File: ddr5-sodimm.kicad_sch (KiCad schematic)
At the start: 31 parts, among them J2 Bus_DDR5_SODIMM_Amphenol_1016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, Q10 BSS138PW, Q11 BSS138PW, Q9 BSS138PW, SW3 SW_KMR211NGLFS_SMD

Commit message: Changing SO-DIMM sch to UDIMM
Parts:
- removed R23, R25: R_47k_0402, antmicro-footprints:R_0402_1005Metric, symbol antmicroResistors0402:R_47k_0402
- removed R24, R26, R27, R28, R29, R30, R32, R33, R34, R35: R_0R_0402, antmicro-footprints:R_0402_1005Metric, symbol antmicroResistors0402:R_0R_0402
- added unit 4 of J2
- J2: footprint antmicro-footprints:Bus_DDR5_SODIMM_Amphenol_10161033-002RHLF -> sodimm-ddr5-tester-footprints:Bus_DDR5_SODIMM_Amphenol_10161033-002RHLF; symbol antmicroMemoryConnectorsPCCardSockets:Bus_DDR5_SODIMM_Amphenol_10161033-002RHLF_CUSTOM_2xDetectPin -> sodimm-ddr5-tester-lib:Bus_DDR5_UDIMM_Amphenol; Author Antmicro -> HimaSava; MPN 10161033-002RHLF -> DDR503112007K
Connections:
- net RFU1 is gone; now on net DDR.SDA: J2.5 (HSDA)
- net +5V: now also J2.145 (VIN_BULK), J2.146 (VIN_BULK), J2.2 (VIN_BULK); no longer J2.3 (VIN_BULK)
- net A.CA0: now also J2.60 (CA0_A); no longer J2.107 (CA0_A)
- net A.CA1: now also J2.204 (CA1_A); no longer J2.109 (CA1_A)
- net A.CA10: now also J2.67 (CA10_A); no longer J2.125 (CA10_A)
- net A.CA11: now also J2.211 (CA11_A); no longer J2.126 (CA11_A)
- net A.CA12: now also J2.69 (CA12_A); no longer J2.127 (CA12_A)
- net A.CA2: now also J2.61 (CA2_A); no longer J2.113 (CA2_A)
- net A.CA3: now also J2.205 (CA3_A); no longer J2.114 (CA3_A)
- net A.CA4: now also J2.63 (CA4_A); no longer J2.115 (CA4_A)
- net A.CA5: now also J2.207 (CA5_A); no longer J2.116 (CA5_A)
- net A.CA6: now also J2.64 (CA6_A); no longer J2.119 (CA6_A)
- net A.CA7: now also J2.208 (CA7_A); no longer J2.120 (CA7_A)
- net A.CA8: now also J2.66 (CA8_A); no longer J2.121 (CA8_A)
- net A.CA9: now also J2.210 (CA9_A); no longer J2.122 (CA9_A)
- net A.CB0: now also J2.51 (CB0_A); no longer J2.95 (CB0_A)
- net A.CB1: now also J2.53 (CB1_A); no longer J2.96 (CB1_A)
- net A.CB2: now also J2.196 (CB2_A); no longer J2.99 (CB2_A)
- net A.CB3: now also J2.198 (CB3_A); no longer J2.103 (CB3_A)
- net A.CK0_N: now also J2.73 (CK0_A_c); no longer J2.133 (CK0_A_c)
- net A.CK0_P: now also J2.72 (CK0_A_t); no longer J2.131 (CK0_A_t)
- net A.CK1_N: now also J2.217 (CK1_A_c); no longer J2.134 (CK1_A_c)
- net A.CK1_P: now also J2.216 (CK1_A_t); no longer J2.132 (CK1_A_t)
- net A.DQ0: now also J2.9 (DQ0_A); no longer J2.11 (DQ0_A)
- net A.DQ1: now also J2.11 (DQ1_A); no longer J2.12 (DQ1_A)
- net A.DQ10: now also J2.164 (DQ10_A); no longer J2.35 (DQ10_A)
- net A.DQ11: now also J2.166 (DQ11_A); no longer J2.38 (DQ11_A)
- net A.DQ12: now also J2.26 (DQ12_A); no longer J2.45 (DQ12_A)
- net A.DQ13: now also J2.28 (DQ13_A); no longer J2.46 (DQ13_A)
- net A.DQ14: now also J2.171 (DQ14_A); no longer J2.49 (DQ14_A)
- net A.DQ15: now also J2.173 (DQ15_A); no longer J2.50 (DQ15_A)
- net A.DQ16: now also J2.30 (DQ16_A); no longer J2.53 (DQ16_A)
- net A.DQ17: now also J2.32 (DQ17_A); no longer J2.54 (DQ17_A)
- net A.DQ18: now also J2.175 (DQ18_A); no longer J2.57 (DQ18_A)
- net A.DQ19: now also J2.177 (DQ19_A); no longer J2.58 (DQ19_A)
- net A.DQ2: now also J2.154 (DQ2_A); no longer J2.15 (DQ2_A)
- net A.DQ20: now also J2.37 (DQ20_A); no longer J2.65 (DQ20_A)
- net A.DQ21: now also J2.39 (DQ21_A); no longer J2.68 (DQ21_A)
- net A.DQ22: now also J2.181 (DQ22_A); no longer J2.69 (DQ22_A)
- net A.DQ23: now also J2.183 (DQ23_A); no longer J2.72 (DQ23_A)
- net A.DQ24: now also J2.41 (DQ24_A); no longer J2.73 (DQ24_A)
- net A.DQ25: now also J2.43 (DQ25_A); no longer J2.76 (DQ25_A)
- net A.DQ26: now also J2.185 (DQ26_A); no longer J2.77 (DQ26_A)
- net A.DQ27: now also J2.187 (DQ27_A); no longer J2.80 (DQ27_A)
- net A.DQ28: now also J2.47 (DQ28_A); no longer J2.87 (DQ28_A)
- net A.DQ29: now also J2.49 (DQ29_A); no longer J2.88 (DQ29_A)
- net A.DQ3: now also J2.156 (DQ3_A); no longer J2.16 (DQ3_A)
- net A.DQ30: now also J2.192 (DQ30_A); no longer J2.91 (DQ30_A)
- net A.DQ31: now also J2.194 (DQ31_A); no longer J2.92 (DQ31_A)
- net A.DQ4: now also J2.16 (DQ4_A); no longer J2.23 (DQ4_A)
- net A.DQ5: now also J2.18 (DQ5_A); no longer J2.26 (DQ5_A)
- net A.DQ6: now also J2.160 (DQ6_A); no longer J2.27 (DQ6_A)
- net A.DQ7: now also J2.162 (DQ7_A); no longer J2.30 (DQ7_A)
- net A.DQ8: now also J2.20 (DQ8_A); no longer J2.31 (DQ8_A)
- net A.DQ9: now also J2.22 (DQ09_A); no longer J2.34 (DQ09_A)
- net A.DQS0_N: now also J2.13 (DQS0_A_C); no longer J2.20 (DQS0_A_C)
- net A.DQS0_P: now also J2.14 (DQS0_A_t); no longer J2.22 (DQS0_A_t)
- net A.DQS1_N: now also J2.168 (DQS1_A_C); no longer J2.39 (DQS1_A_C)
- net A.DQS1_P: now also J2.169 (DQS1_A_t); no longer J2.41 (DQS1_A_t)
- net A.DQS2_N: now also J2.34 (DQS2_A_C); no longer J2.62 (DQS2_A_C)
- net A.DQS2_P: now also J2.35 (DQS2_A_t); no longer J2.64 (DQS2_A_t)
- net A.DQS3_N: now also J2.189 (DQS3_A_C); no longer J2.81 (DQS3_A_C)
- net A.DQS3_P: now also J2.190 (DQS3_A_t); no longer J2.83 (DQS3_A_t)
- net A.DQS4_N: now also J2.55 (DQS4_A_c); no longer J2.100 (DQS4_A_c)
- net A.DQS4_P: now also J2.56 (DQS4_A_t); no longer J2.102 (DQS4_A_t)
- net A.~{CS0}: now also J2.58 (CS0_A_n); no longer J2.106 (CS0_A_n)
- net A.~{CS1}: now also J2.202 (CS1_A_n); no longer J2.110 (CS1_A_n)
- net A.~{DM0}: now also J2.158 (DM0_A_n); no longer J2.19 (DM0_A_n)
- net A.~{DM1}: now also J2.24 (DM1_A_n); no longer J2.42 (DM1_A_n)
- net A.~{DM2}: now also J2.179 (DM2_A_n); no longer J2.61 (DM2_A_n)
- net A.~{DM3}: now also J2.45 (DM3_A_n); no longer J2.84 (DM3_A_n)
- net B.CA0: now also J2.91 (CA0_B); no longer J2.164 (CA0_B)
- net B.CA1: now also J2.235 (CA1_B); no longer J2.162 (CA1_B)
- net B.CA10: now also J2.84 (CA10_B); no longer J2.146 (CA10_B)
- net B.CA11: now also J2.228 (CA11_B); no longer J2.145 (CA11_B)
- net B.CA12: now also J2.82 (CA12_B); no longer J2.144 (CA12_B)
- net B.CA2: now also J2.90 (CA2_B); no longer J2.158 (CA2_B)
- net B.CA3: now also J2.234 (CA3_B); no longer J2.157 (CA3_B)
- net B.CA4: now also J2.88 (CA4_B); no longer J2.156 (CA4_B)
- net B.CA5: now also J2.232 (CA5_B); no longer J2.155 (CA5_B)
- net B.CA6: now also J2.87 (CA6_B); no longer J2.152 (CA6_B)
- net B.CA7: now also J2.231 (CA7_B); no longer J2.151 (CA7_B)
- net B.CA8: now also J2.85 (CA8_B); no longer J2.150 (CA8_B)
- net B.CA9: now also J2.229 (CA9_B); no longer J2.149 (CA9_B)
- net B.CB0: now also J2.97 (CB0_B); no longer J2.168 (CB0_B)
- net B.CB1: now also J2.99 (CB1_B); no longer J2.172 (CB1_B)
- net B.CB2: now also J2.242 (CB2_B); no longer J2.176 (CB2_B)
- net B.CB3: now also J2.244 (CB3_B); no longer J2.175 (CB3_B)
- net B.CK0_N: now also J2.79 (CK0_B_c); no longer J2.139 (CK0_B_c)
- net B.CK0_P: now also J2.78 (CK0_B_t); no longer J2.137 (CK0_B_t)
- net B.CK1_N: now also J2.223 (CK1_B_C); no longer J2.140 (CK1_B_C)
- net B.CK1_P: now also J2.222 (CK1_B_t); no longer J2.138 (CK1_B_t)
- net B.DQ0: now also J2.101 (DQ0_B); no longer J2.179 (DQ0_B)
- net B.DQ1: now also J2.103 (DQ1_B); no longer J2.180 (DQ1_B)
- net B.DQ10: now also J2.256 (DQ10_B); no longer J2.203 (DQ10_B)
- net B.DQ11: now also J2.258 (DQ11_B); no longer J2.206 (DQ11_B)
- net B.DQ12: now also J2.118 (DQ12_B); no longer J2.213 (DQ12_B)
- net B.DQ13: now also J2.120 (DQ13_B); no longer J2.214 (DQ13_B)
- net B.DQ14: now also J2.263 (DQ14_B); no longer J2.217 (DQ14_B)
- net B.DQ15: now also J2.265 (DQ15_B); no longer J2.218 (DQ15_B)
- net B.DQ16: now also J2.122 (DQ16_B); no longer J2.221 (DQ16_B)
- net B.DQ17: now also J2.124 (DQ17_B); no longer J2.222 (DQ17_B)
- net B.DQ18: now also J2.267 (DQ18_B); no longer J2.225 (DQ18_B)
- net B.DQ19: now also J2.269 (DQ19_B); no longer J2.226 (DQ19_B)
- net B.DQ2: now also J2.246 (DQ2_B); no longer J2.183 (DQ2_B)
- net B.DQ20: now also J2.129 (DQ20_B); no longer J2.233 (DQ20_B)
- net B.DQ21: now also J2.131 (DQ21_B); no longer J2.236 (DQ21_B)
- net B.DQ22: now also J2.273 (DQ22_B); no longer J2.237 (DQ22_B)
- net B.DQ23: now also J2.275 (DQ23_B); no longer J2.240 (DQ23_B)
- net B.DQ24: now also J2.133 (DQ24_B); no longer J2.241 (DQ24_B)
- net B.DQ25: now also J2.135 (DQ25_B); no longer J2.244 (DQ25_B)
- net B.DQ26: now also J2.277 (DQ26_B); no longer J2.245 (DQ26_B)
- net B.DQ27: now also J2.279 (DQ27_B); no longer J2.248 (DQ27_B)
- net B.DQ28: now also J2.139 (DQ28_B); no longer J2.255 (DQ28_B)
- net B.DQ29: now also J2.141 (DQ29_B); no longer J2.256 (DQ29_B)
- net B.DQ3: now also J2.248 (DQ3_B); no longer J2.184 (DQ3_B)
- net B.DQ30: now also J2.284 (DQ30_B); no longer J2.259 (DQ30_B)
- net B.DQ31: now also J2.286 (DQ31_B); no longer J2.260 (DQ31_B)
- net B.DQ4: now also J2.108 (DQ4_B); no longer J2.191 (DQ4_B)
- net B.DQ5: now also J2.110 (DQ5_B); no longer J2.194 (DQ5_B)
- net B.DQ6: now also J2.252 (DQ6_B); no longer J2.195 (DQ6_B)
- net B.DQ7: now also J2.254 (DQ7_B); no longer J2.198 (DQ7_B)
- net B.DQ8: now also J2.112 (DQ8_B); no longer J2.199 (DQ8_B)
- net B.DQ9: now also J2.114 (DQ9_B); no longer J2.202 (DQ9_B)
- net B.DQS0_N: now also J2.105 (DQS0_B_C); no longer J2.188 (DQS0_B_C)
- net B.DQS0_P: now also J2.106 (DQS0_B_t); no longer J2.190 (DQS0_B_t)
- net B.DQS1_N: now also J2.260 (DQS1_B_C); no longer J2.207 (DQS1_B_C)
- net B.DQS1_P: now also J2.261 (DQS1_B_t); no longer J2.209 (DQS1_B_t)
- net B.DQS2_N: now also J2.126 (DQS2_B_C); no longer J2.230 (DQS2_B_C)
- net B.DQS2_P: now also J2.127 (DQS2_B_t); no longer J2.232 (DQS2_B_t)
- net B.DQS3_N: now also J2.281 (DQS3_B_c); no longer J2.249 (DQS3_B_c)
- net B.DQS3_P: now also J2.282 (DQS3_B_t); no longer J2.251 (DQS3_B_t)
- net B.DQS4_N: now also J2.239 (DQS4_B_c); no longer J2.169 (DQS4_B_c)
- net B.DQS4_P: now also J2.240 (DQS4_B_T); no longer J2.171 (DQS4_B_T)
- net B.~{CS0}: now also J2.93 (CS0_B_n); no longer J2.161 (CS0_B_n)
- net B.~{CS1}: now also J2.237 (CS1_B_N); no longer J2.165 (CS1_B_N)
- net B.~{DM0}: now also J2.250 (DM0_B_n); no longer J2.187 (DM0_B_n)
- net B.~{DM1}: now also J2.116 (DM1_B_n); no longer J2.210 (DM1_B_n)
- net B.~{DM2}: now also J2.271 (DM2_B_n); no longer J2.229 (DM2_B_n)
- net B.~{DM3}: now also J2.137 (DM3_B_n); no longer J2.252 (DM3_B_n)
- net Control.~{ALERT}: now also J2.200 (ALERT_n); no longer J2.108 (ALERT_n)
- net Control.~{RESET}: now also J2.95 (RESET_n); no longer J2.163 (RESET_n)
- net DDR.SDA: no longer J2.6 (HSDA)
- net GND: now also J2.10 (Vss), J2.100 (Vss), J2.102 (Vss), J2.104 (Vss), J2.107 (Vss), J2.109 (Vss), J2.111 (Vss), J2.113 (Vss), J2.115 (Vss), J2.117 (Vss), J2.119 (Vss), J2.12 (Vss), J2.121 (Vss), J2.123 (Vss), J2.125 (Vss), J2.128 (Vss), J2.130 (Vss), J2.132 (Vss), J2.134 (Vss), J2.136 (Vss), J2.138 (Vss), J2.140 (Vss), J2.142 (Vss), J2.15 (Vss), J2.150 (Vss), J2.153 (Vss), J2.155 (Vss), J2.157 (Vss), J2.159 (Vss), J2.161 (Vss), J2.163 (Vss), J2.165 (Vss), J2.167 (Vss), J2.17 (Vss), J2.170 (Vss), J2.172 (Vss), J2.174 (Vss), J2.176 (Vss), J2.178 (Vss), J2.180 (Vss), J2.182 (Vss), J2.184 (Vss), J2.186 (Vss), J2.188 (Vss), J2.19 (Vss), J2.191 (Vss), J2.193 (Vss), J2.195 (Vss), J2.197 (Vss), J2.199 (Vss), J2.201 (Vss), J2.203 (Vss), J2.206 (Vss), J2.209 (Vss), J2.21 (Vss), J2.212 (Vss), J2.215 (Vss), J2.218 (Vss), J2.221 (Vss), J2.224 (Vss), J2.227 (Vss), J2.23 (Vss), J2.230 (Vss), J2.233 (Vss), J2.236 (Vss), J2.238 (Vss), J2.241 (Vss), J2.243 (Vss), J2.245 (Vss), J2.247 (Vss), J2.249 (Vss), J2.25 (Vss), J2.251 (Vss), J2.253 (Vss), J2.255 (Vss), J2.257 (Vss), J2.259 (Vss), J2.262 (Vss), J2.264 (Vss), J2.266 (Vss), J2.268 (Vss), J2.27 (Vss), J2.270 (Vss), J2.272 (Vss), J2.274 (Vss), J2.276 (Vss), J2.278 (Vss), J2.280 (Vss), J2.283 (Vss), J2.285 (Vss), J2.287 (Vss), J2.29 (Vss), J2.31 (Vss), J2.33 (Vss), J2.36 (Vss), J2.38 (Vss), J2.40 (Vss), J2.42 (Vss), J2.44 (Vss), J2.46 (Vss), J2.48 (Vss), J2.50 (Vss), J2.52 (Vss), J2.54 (Vss), J2.57 (Vss), J2.59 (Vss), J2.6 (Vss), J2.62 (Vss), J2.65 (Vss), J2.68 (Vss), J2.71 (Vss), J2.74 (Vss), J2.77 (Vss), J2.8 (Vss), J2.80 (Vss), J2.83 (Vss), J2.86 (Vss), J2.89 (Vss), J2.92 (Vss), J2.94 (Vss), J2.96 (Vss), J2.98 (Vss); no longer J2.10 (VSS), J2.101 (VSS), J2.104 (VSS), J2.105 (VSS), J2.111 (VSS), J2.112 (VSS), J2.117 (VSS), J2.118 (VSS), J2.123 (VSS), J2.129 (VSS), J2.13 (VSS), J2.135 (VSS), J2.136 (VSS), J2.14 (VSS), J2.141 (VSS), J2.142 (VSS), J2.147 (VSS), J2.148 (VSS), J2.153 (VSS), J2.154 (VSS), J2.159 (VSS), J2.160 (VSS), J2.166 (VSS), J2.167 (VSS), J2.17 (VSS), J2.170 (VSS), J2.173 (VSS), J2.174 (VSS), J2.177 (VSS), J2.178 (VSS), J2.18 (VSS), J2.181 (VSS), J2.182 (VSS), J2.185 (VSS), J2.186 (VSS), J2.189 (VSS), J2.192 (VSS), J2.193 (VSS), J2.196 (VSS), J2.197 (VSS), J2.200 (VSS), J2.201 (VSS), J2.204 (VSS), J2.205 (VSS), J2.208 (VSS), J2.21 (VSS), J2.211 (VSS), J2.212 (VSS), J2.215 (VSS), J2.216 (VSS), J2.219 (VSS), J2.220 (VSS), J2.223 (VSS), J2.224 (VSS), J2.227 (VSS), J2.228 (VSS), J2.231 (VSS), J2.234 (VSS), J2.235 (VSS), J2.238 (VSS), J2.239 (VSS), J2.24 (VSS), J2.242 (VSS), J2.243 (VSS), J2.246 (VSS), J2.247 (VSS), J2.25 (VSS), J2.250 (VSS), J2.253 (VSS), J2.254 (VSS), J2.257 (VSS), J2.258 (VSS), J2.261 (VSS), J2.262 (VSS), J2.28 (VSS), J2.29 (VSS), J2.32 (VSS), J2.33 (VSS), J2.36 (VSS), J2.37 (VSS), J2.40 (VSS), J2.43 (VSS), J2.44 (VSS), J2.47 (VSS), J2.48 (VSS), J2.51 (VSS), J2.52 (VSS), J2.55 (VSS), J2.56 (VSS), J2.59 (VSS), J2.60 (VSS), J2.63 (VSS), J2.66 (VSS), J2.67 (VSS), J2.70 (VSS), J2.71 (VSS), J2.74 (VSS), J2.75 (VSS), J2.78 (VSS), J2.79 (VSS), J2.82 (VSS), J2.85 (VSS), J2.86 (VSS), J2.89 (VSS), J2.9 (VSS), J2.90 (VSS), J2.93 (VSS), J2.94 (VSS), J2.97 (VSS), J2.98 (VSS), J2.SH
- net HSA: now also J2.148 (HSA); no longer J2.2 (HSA)
- net at R38.1: now also J2.151 (PWR_EN); no longer J2.8 (PWR_EN)
- net at R31.2: now also J2.147 (PWR_GOOD); no longer J2.7 (PWR_GOOD)
- removed net RFU2: J2.128 (RFU)
- removed net RFU3: J2.143 (RFU)
- removed net VSS_DET1: J2.124 (SDM_DETECT)
- removed net VSS_DET2: J2.130 (TB_DETECT)
- no-connect marks 0 -> 20
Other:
- note added: "Ground and RFU"
- note removed: "0"
- note removed: "1"
- note removed: "Antmicro Testbed"
- note removed: "DDR5 SO-DIMM"
- note removed: "Not populated"
- note removed: "Optional RFU"
- note removed: "SO-DIMM type detect"
- note removed: "TB_DETECT"
- note removed: "~{DDR_PRESENCE}"
- moved on the sheet: C10, C127, C6, C7, C8, C9, J2A, J2B, R128, R31, R38, R78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

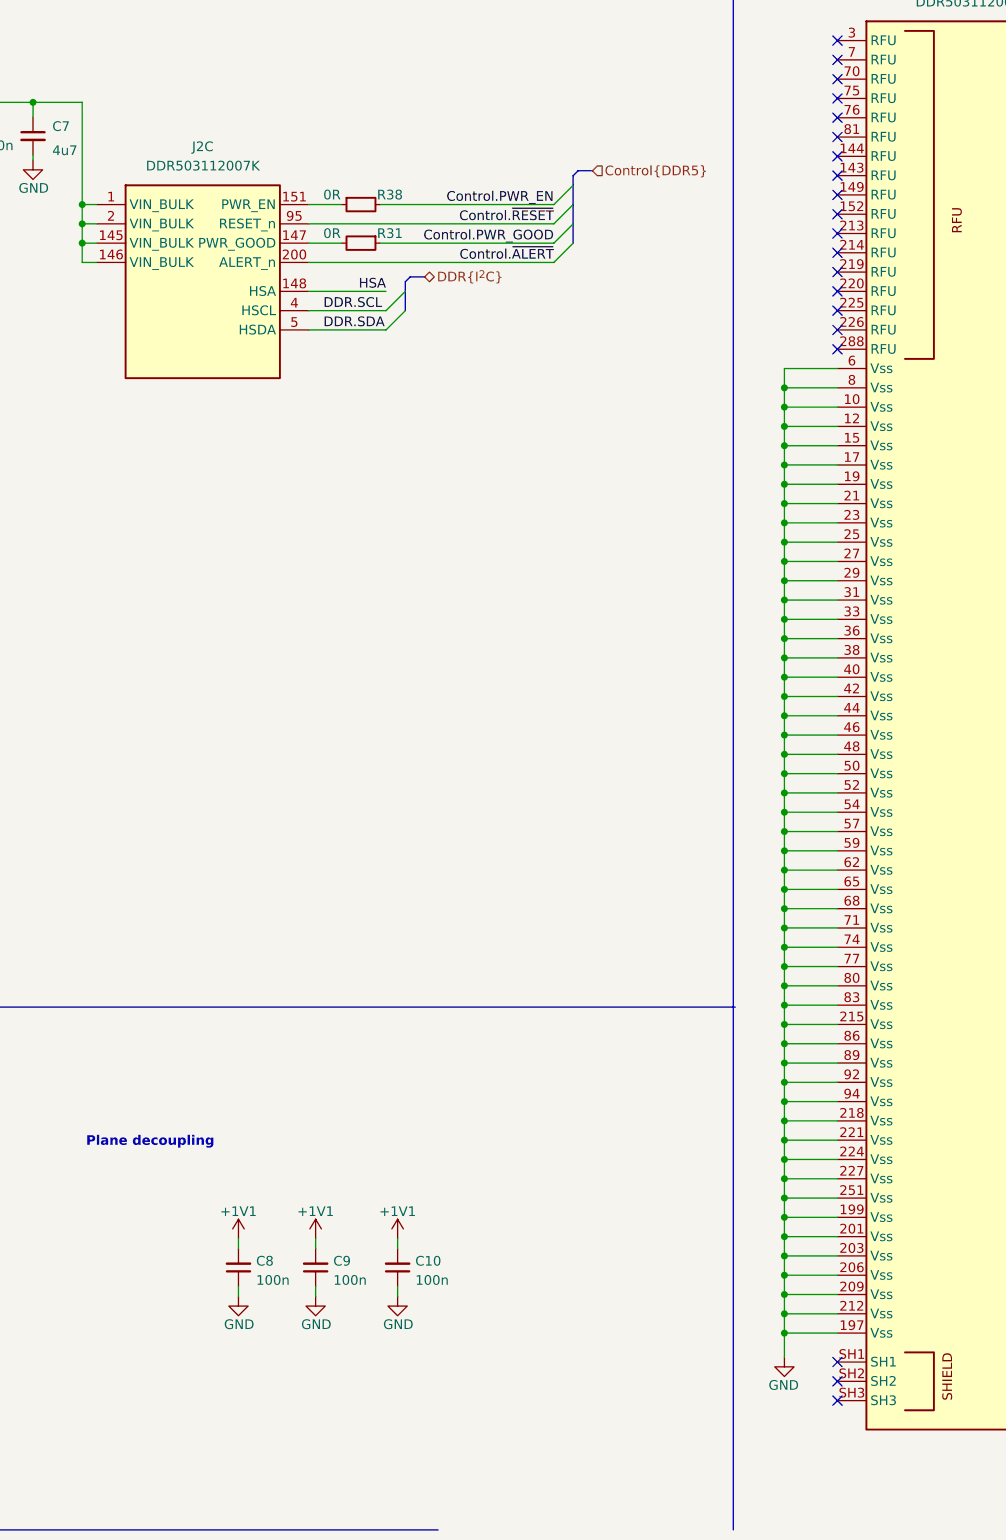
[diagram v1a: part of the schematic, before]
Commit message: Changing DDR sch and PCB
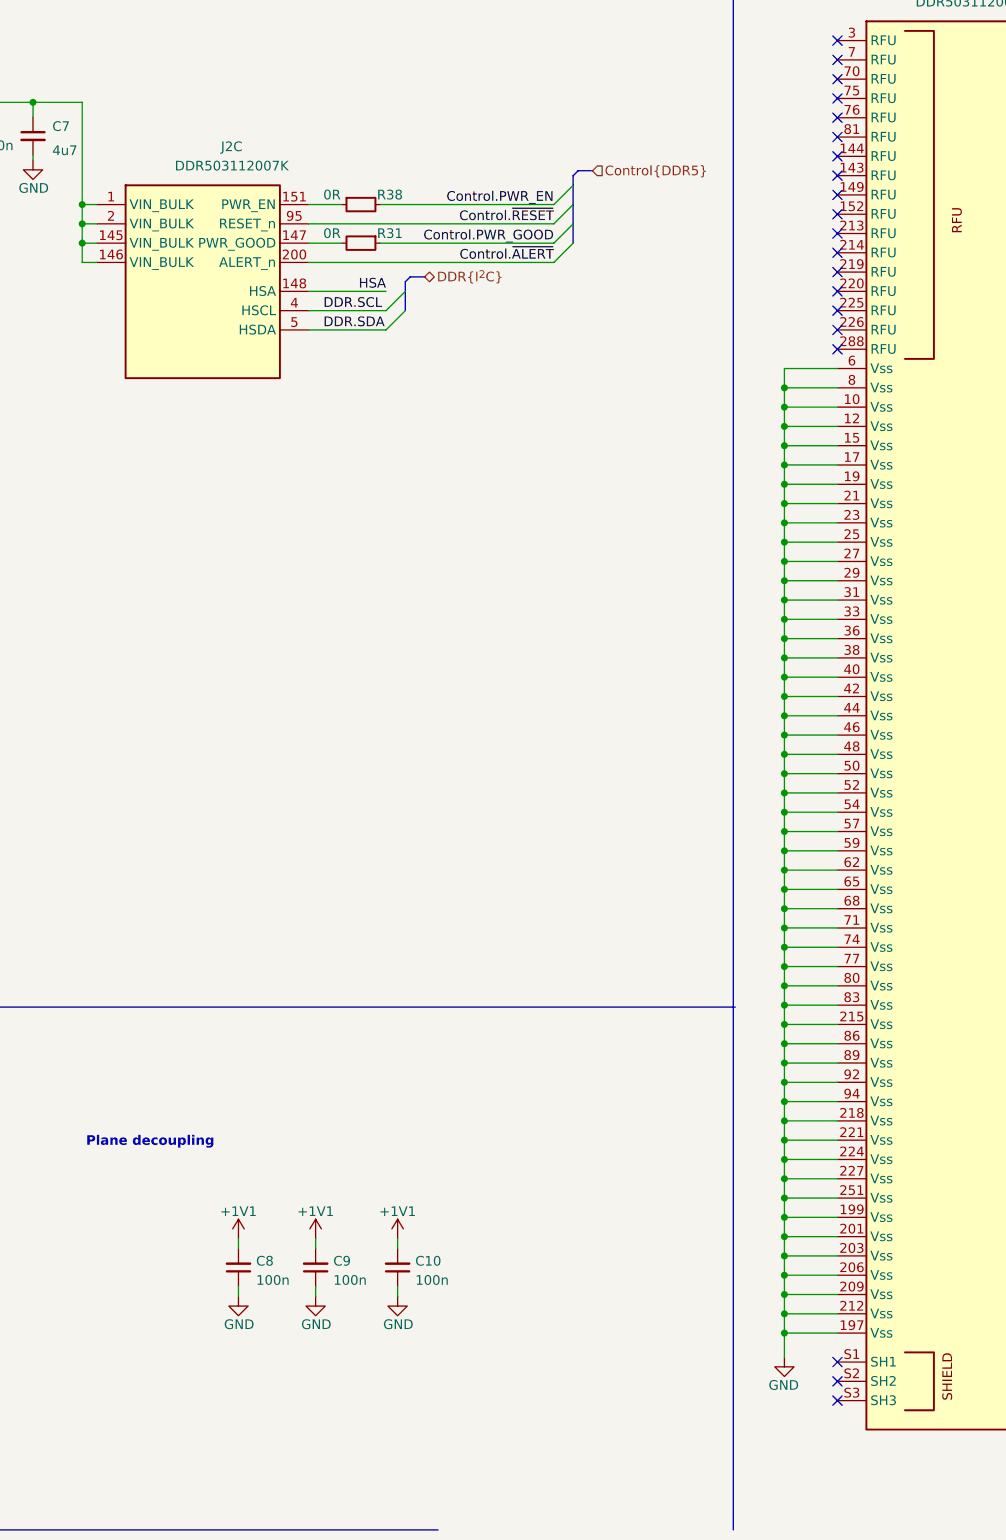
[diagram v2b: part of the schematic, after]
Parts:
- J2: value Bus_DDR5_SODIMM_Amphenol_10161033-002RHLF_CUSTOM_2xDetectPin -> Bus_DDR5_UDIMM_Amphenol; footprint sodimm-ddr5-tester-footprints:Bus_DDR5_SODIMM_Amphenol_10161033-002RHLF -> sodimm-ddr5-tester-footprints:Bus_DDR5_Socket_Amphenol_DDR503112007K
- J2: footprint sodimm-ddr5-tester-footprints:Bus_DDR5_SODIMM_Amphenol_10161033-002RHLF -> sodimm-ddr5-tester-footprints:Bus_DDR5_Socket_Amphenol_DDR503112007K
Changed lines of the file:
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@@
     )
   )
-  (symbol (lib_id "sodimm-ddr5-tester-lib:Bus_DDR5_UDIMM_Amphenol") (at 153.924 46.99 0) (unit 2)
+  (symbol (lib_name "Bus_DDR5_UDIMM_Amphenol_3") (lib_id "sodimm-ddr5-tester-lib:Bus_DDR5_UDIMM_Amphenol") (at 153.924 46.99 0) (unit 2)
     (in_bom yes) (on_board yes) (dnp no) (fields_autoplaced)
     (property "Reference" "J2" (at 171.704 39.37 0)
       (effects (font (size 1.27 1.27) (thickness 0.15)))
     )
-    (property "Value" "Bus_DDR5_SODIMM_Amphenol_10161033-002RHLF_CUSTOM_2xDetectPin" (at 204.724 54.61 0)
-      (effects (font (size 1.27 1.27) (thickness 0.15)) (justify left bottom) hide)
-    )
-    (property "Footprint" "sodimm-ddr5-tester-footprints:Bus_DDR5_SODIMM_Amphenol_10161033-002RHLF" (at 204.724 57.15 0)
+    (property "Value" "Bus_DDR5_UDIMM_Amphenol" (at 204.724 54.61 0)
+      (effects (font (size 1.27 1.27) (thickness 0.15)) (justify left bottom) hide)
+    )
+    (property "Footprint" "sodimm-ddr5-tester-footprints:Bus_DDR5_Socket_Amphenol_DDR503112007K" (at 204.724 57.15 0)
       (effects (font (size 1.27 1.27) (thickness 0.15)) (justify left bottom) hide)
     )
@@
     (pin "286")
     (pin "279")
-    (pin "SH3")
+    (pin "S1")
     (pin "280")
     (pin "272")
-    (pin "SH2")
+    (pin "S3")
     (pin "268")
     (pin "264")
-    (pin "SH1")
+    (pin "S2")
     (pin "287")
     (pin "278")
@@
       (effects (font (size 1.27 1.27) (thickness 0.15)) (justify left bottom) hide)
     )
-    (property "Footprint" "sodimm-ddr5-tester-footprints:Bus_DDR5_SODIMM_Amphenol_10161033-002RHLF" (at 403.352 67.056 0)
+    (property "Footprint" "sodimm-ddr5-tester-footprints:Bus_DDR5_Socket_Amphenol_DDR503112007K" (at 403.352 67.056 0)
       (effects (font (size 1.27 1.27) (thickness 0.15)) (justify left bottom) hide)
     )
@@
     (pin "83")
     (pin "89")
-    (pin "SH3")
+    (pin "S1")
     (pin "86")
     (pin "92")
     (pin "96")
-    (pin "SH1")
-    (pin "SH2")
+    (pin "S3")
+    (pin "S2")
     (pin "16")
     (pin "177")
@@
     )
   )
-  (symbol (lib_id "sodimm-ddr5-tester-lib:Bus_DDR5_UDIMM_Amphenol") (at 255.016 78.486 0) (unit 3)
+  (symbol (lib_name "Bus_DDR5_UDIMM_Amphenol_1") (lib_id "sodimm-ddr5-tester-lib:Bus_DDR5_UDIMM_Amphenol") (at 255.016 78.486 0) (unit 3)
     (in_bom yes) (on_board yes) (dnp no) (fields_autoplaced)
-    (property "Reference" "J2" (at 268.986 70.866 0)
+    (property "Reference" "J2" (at 272.796 70.866 0)
       (effects (font (size 1.27 1.27) (thickness 0.15)))
     )
-    (property "Value" "Bus_DDR5_SODIMM_Amphenol_10161033-002RHLF_CUSTOM_2xDetectPin" (at 305.816 86.106 0)
-      (effects (font (size 1.27 1.27) (thickness 0.15)) (justify left bottom) hide)
-    )
-    (property "Footprint" "sodimm-ddr5-tester-footprints:Bus_DDR5_SODIMM_Amphenol_10161033-002RHLF" (at 305.816 88.646 0)
+    (property "Value" "Bus_DDR5_UDIMM_Amphenol" (at 305.816 86.106 0)
+      (effects (font (size 1.27 1.27) (thickness 0.15)) (justify left bottom) hide)
+    )
+    (property "Footprint" "sodimm-ddr5-tester-footprints:Bus_DDR5_Socket_Amphenol_DDR503112007K" (at 305.816 88.646 0)
       (effects (font (size 1.27 1.27) (thickness 0.15)) (justify left bottom) hide)
     )
@@
       (effects (font (size 1.27 1.27) (thickness 0.15)) (justify left bottom) hide)
     )
-    (property "MPN" "DDR503112007K" (at 268.986 73.406 0)
+    (property "MPN" "DDR503112007K" (at 272.796 73.406 0)
       (effects (font (size 1.27 1.27) (thickness 0.15)))
     )
@@
     (pin "97")
     (pin "98")
-    (pin "SH3")
-    (pin "SH1")
-    (pin "SH2")
+    (pin "S3")
+    (pin "S1")
+    (pin "S2")
     (pin "286")
     (pin "284")
@@
     )
   )
-  (symbol (lib_id "sodimm-ddr5-tester-lib:Bus_DDR5_UDIMM_Amphenol") (at 46.736 46.228 0) (unit 1)
+  (symbol (lib_name "Bus_DDR5_UDIMM_Amphenol_2") (lib_id "sodimm-ddr5-tester-lib:Bus_DDR5_UDIMM_Amphenol") (at 46.736 46.228 0) (unit 1)
     (in_bom yes) (on_board yes) (dnp no) (fields_autoplaced)
     (property "Reference" "J2" (at 64.516 38.608 0)
       (effects (font (size 1.27 1.27) (thickness 0.15)))
     )
-    (property "Value" "Bus_DDR5_SODIMM_Amphenol_10161033-002RHLF_CUSTOM_2xDetectPin" (at 97.536 53.848 0)
-      (effects (font (size 1.27 1.27) (thickness 0.15)) (justify left bottom) hide)
-    )
-    (property "Footprint" "sodimm-ddr5-tester-footprints:Bus_DDR5_SODIMM_Amphenol_10161033-002RHLF" (at 97.536 56.388 0)
+    (property "Value" "Bus_DDR5_UDIMM_Amphenol" (at 97.536 53.848 0)
+      (effects (font (size 1.27 1.27) (thickness 0.15)) (justify left bottom) hide)
+    )
+    (property "Footprint" "sodimm-ddr5-tester-footprints:Bus_DDR5_Socket_Amphenol_DDR503112007K" (at 97.536 56.388 0)
       (effects (font (size 1.27 1.27) (thickness 0.15)) (justify left bottom) hide)
     )
@@
     (pin "268")
     (pin "283")
-    (pin "SH1")
+    (pin "S2")
     (pin "280")
     (pin "287")
@@
     (pin "264")
     (pin "278")
-    (pin "SH2")
-    (pin "SH3")
+    (pin "S1")
+    (pin "S3")
     (pin "273")
     (pin "263")
